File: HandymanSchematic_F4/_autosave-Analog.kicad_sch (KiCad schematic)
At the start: 47 parts, among them Q1 BC847, U1 TL074, U2 TL074

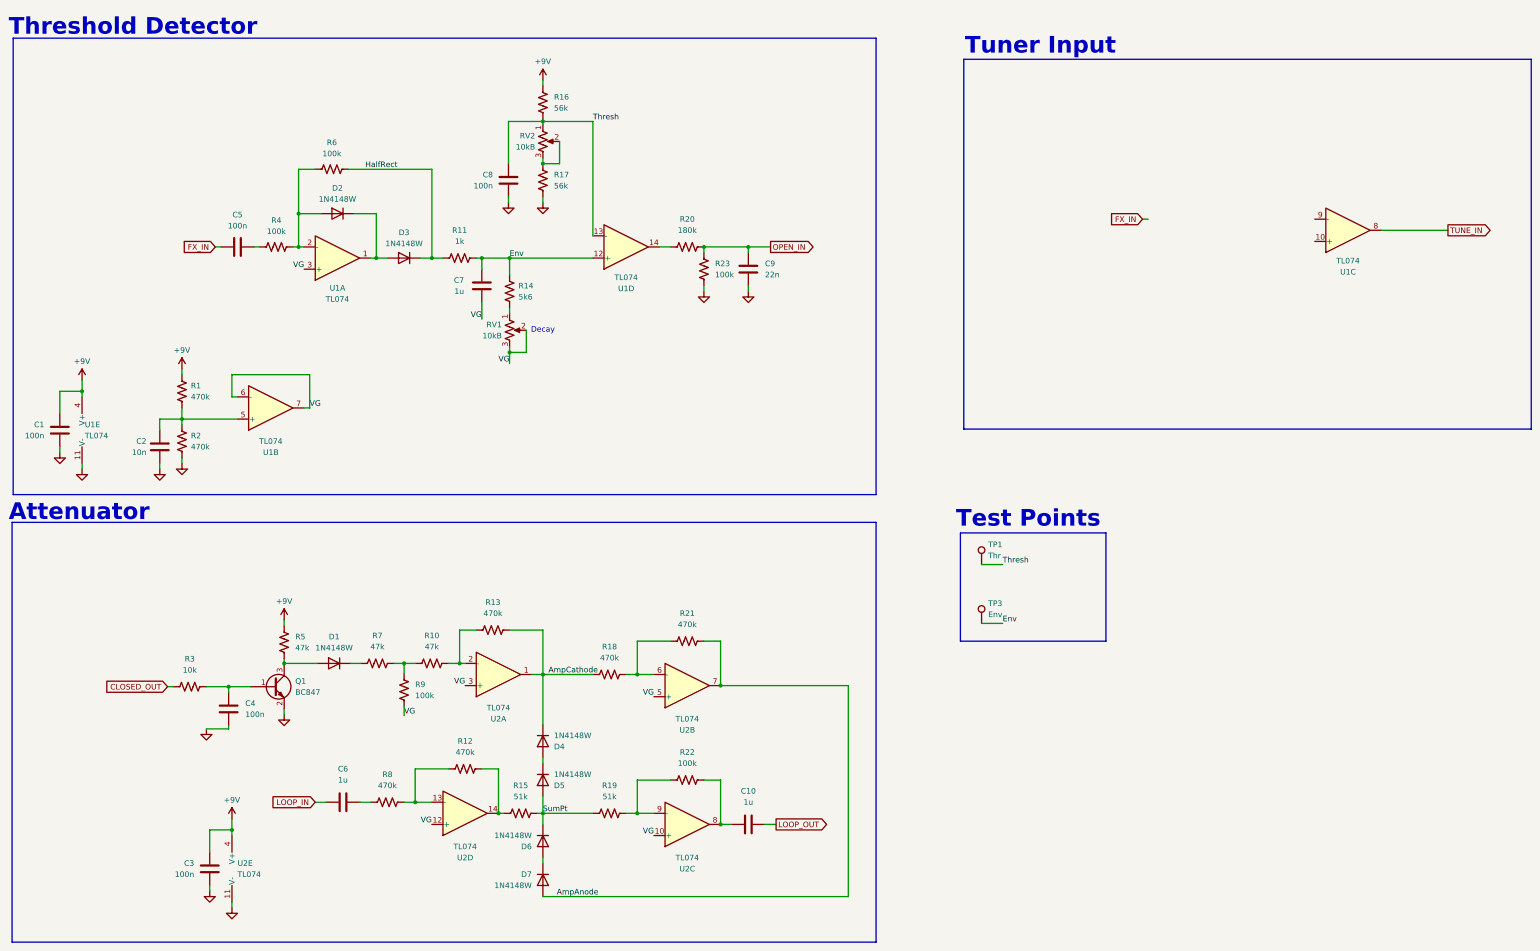
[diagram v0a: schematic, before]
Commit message: attenuator simulation in kicad
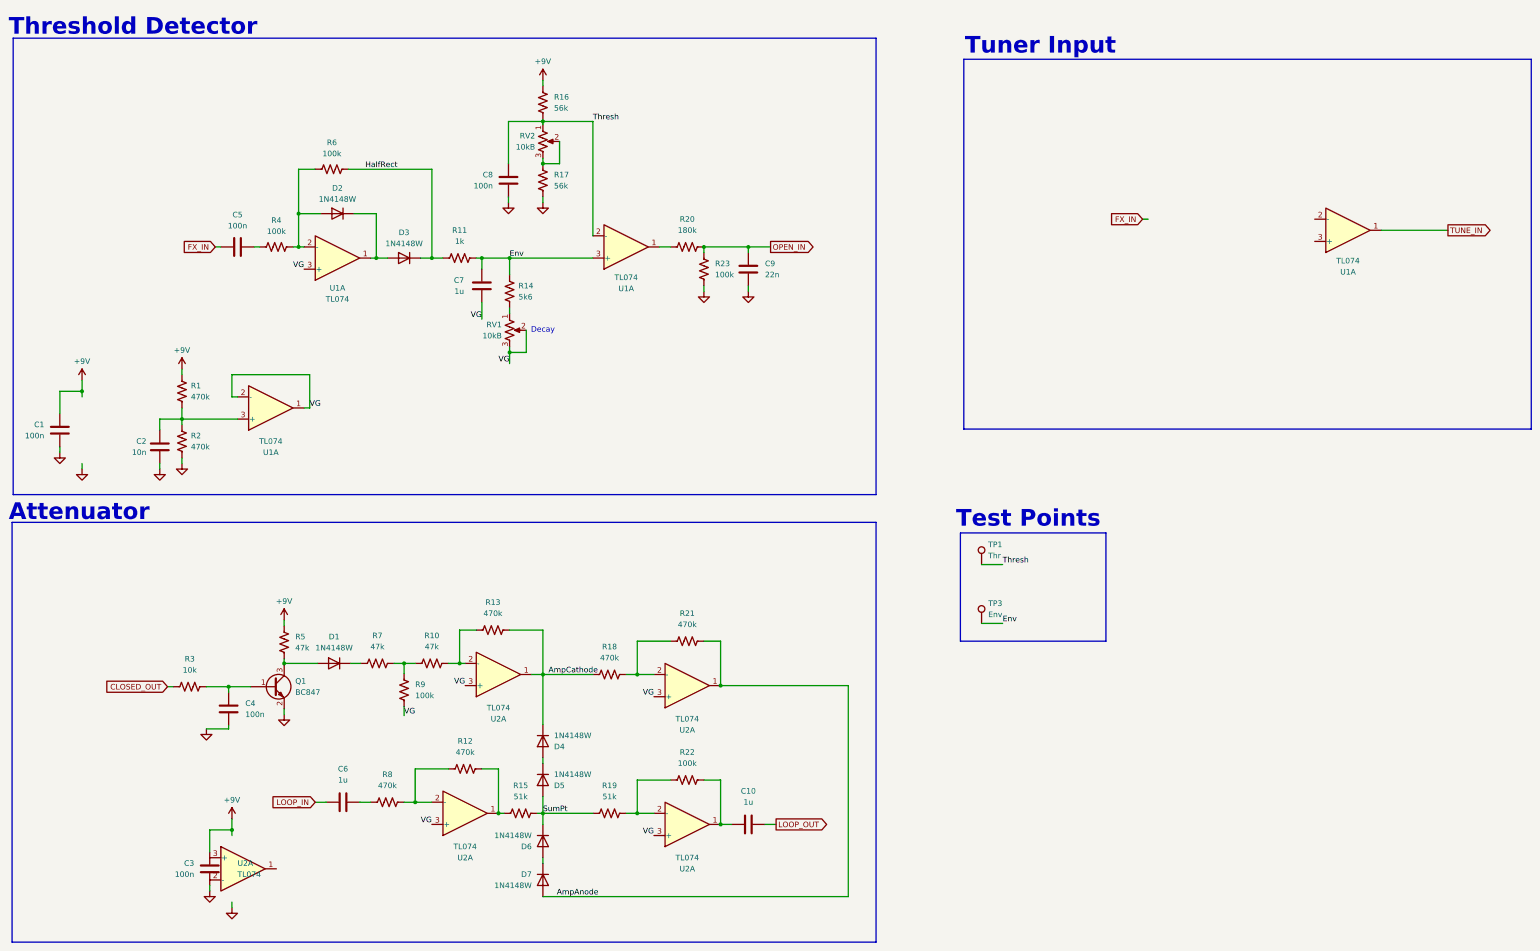
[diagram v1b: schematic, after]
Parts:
- removed unit 5 of U1
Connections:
- net +9V: no longer U2.4 (V+)
- net AmpAnode: now also U2.1; no longer U2.7
- net Env: now also U1.3 (+); no longer U1.12 (+)
- net GND: no longer U2.11 (V-)
- net TUNE_IN: now also U1.1; no longer U1.8
- net Thresh: now also U1.2 (-); no longer U1.13 (-)
- net VG: now also U1.1, U1.2 (-), U2.3 (+), U2.3 (+), U2.3 (+); no longer U1.6 (-), U1.7, U2.10 (+), U2.12 (+), U2.5 (+)
- net at R19.2, R22.1: now also U2.2 (-); no longer U2.9 (-)
- net at C2.1, R1.2, R2.1: now also U1.3 (+); no longer U1.5 (+)
- net at R18.2, R21.1: now also U2.2 (-); no longer U2.6 (-)
- net at R12.1, R8.2: now also U2.2 (-); no longer U2.13 (-)
- net at R12.2, R15.1: now also U2.1; no longer U2.14
- net at C10.1, R22.2: now also U2.1; no longer U2.8
- net at R20.1: now also U1.1; no longer U1.14
